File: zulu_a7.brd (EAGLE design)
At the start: 61 x 25.4 mm, 183 parts, among them J1 Pmod 2x6, Q1 12MHz 25ppm (FPGA + FT2232HQ), Q2 2N7002, Q3 MBT3904DW1T1, U1 XC7A35T-1CPG236C, U10 93LC46BT-I/SN, U2 FT2232HQ USB-UART/JTAG Bridge, U3 AS4C32M16SB-6TIN, U4 W25Q128JVSIQ, U8 LTC3569EUDC#TRPBF, X1 Molex 105017-0001 Micro-USB-B

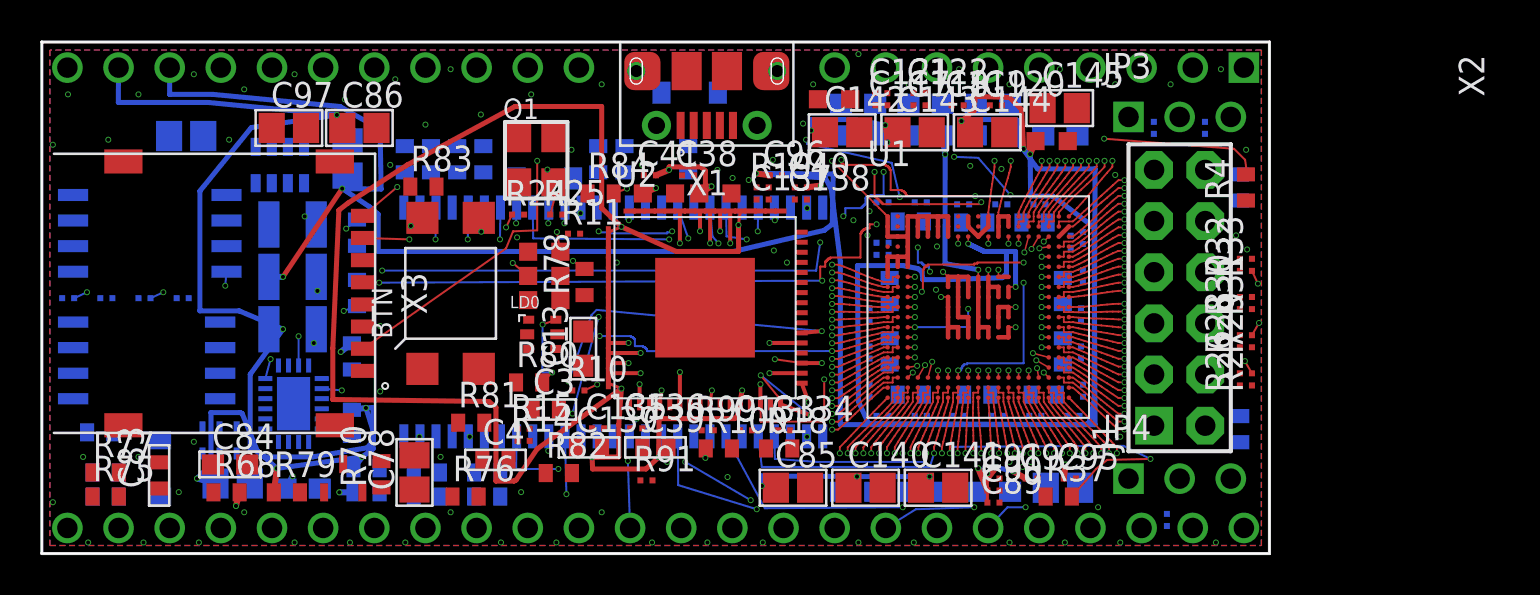
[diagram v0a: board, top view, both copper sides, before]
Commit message: The USB differential pair routes: five faults, each hidden by the one before it
USB_D_P/USB_D_N goes down on L16 at 21.6/21.6 mm, skew 0.921 against a
1.27 mm budget, coupled at exactly 0.2750 mm centre to centre for its whole
length, 0.15 mm conductors, L1 fan-in / L16 coupled / L3 for the side swap.
AIN15 and AIN16 come with it as ordinary single-ended nets, which is right
for XADC inputs at 1 MSPS. 20 of 175 signals bare, against 24; 2620 wires,
408 vias, 0 findings.

Nothing here was congestion. Every one of these was found only after the
previous one stopped masking it.

1. THE FAN-OUT WAS NEVER WIDENED. The two vias at an end sit where their
conductors end, PAIR_W + PAIR_GAP = 0.275 mm apart, and two 0.30 mm vias at
0.09 need 0.390. route_pair's docstring has promised since it was written
that "the fan-out is widened if it does not hold" -- it measured the gap,
reported it and gave up, and the worked example it quoted assumed the older
0.20/0.20 = 0.400 from before PAIR_W and PAIR_GAP were set for 90 ohm.
Every pair on the board died here. The ends are splayed to 0.390 now,
0.0575 mm per conductor, tapering back over the first segment; the coupled
section keeps its gap and its impedance, and an end is coupled to nothing
because it is about to become a via.

2. THE SIDE SWAP WAS COMPUTED AND DISCARDED. crossover() runs for either
branch -- it is what answers a reversed pad order, and this pair has one:
D- is left of D+ at U2 and right of it at X1 -- but only the padlay == lay
branch used the result. The other branch rebuilt A's segments from the
polyline, keeping the exact segment the layer change exists to replace, and
dropped xvias and xsegs. That branch is this pair's case: pads on L1,
coupled on L3. Symptom was "the two conductors come within 0.0000 mm".

3. VIA OWNERSHIP WAS SPLIT BY POSITION. return {pa: vias[:2], pb: vias[2:]}
is right only while each conductor has exactly two vias in that order.
Adding the crossover's broke it silently: USB_D_N came out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
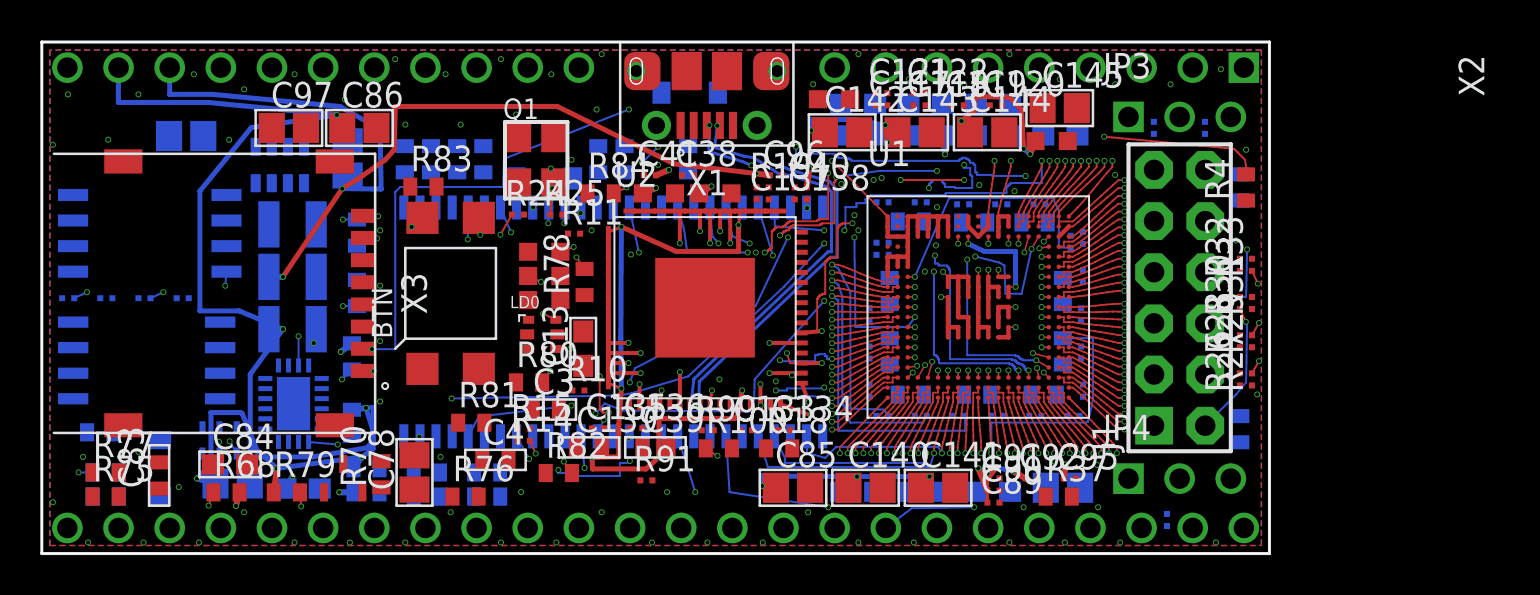
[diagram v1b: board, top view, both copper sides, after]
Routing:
- net VCC1V8: track 221.6 -> 144.0 mm
- net CHAN27: track 67.8 -> 4.05 mm, vias 3 -> 1
- net CHAN19: track 65.9 -> 3.09 mm, vias 5 -> 1
- net CHAN20: track 61.3 -> 3.91 mm, vias 5 -> 1
- net CHAN22: track 2.96 -> 57.8 mm, vias 1 -> 4
- net CHAN11: track 51.7 -> 0.35 mm, vias 4 -> 1
- net JA7: track 0.71 -> 46.1 mm, vias 1 -> 5
- net SD-CLK: track 45.2 -> 0.35 mm, vias 5 -> 1
- net FT-VCORE: track 77.7 -> 35.6 mm
- net CHAN21: track 0.35 -> 39.0 mm, vias 1 -> 4
- net SW2_NET: track 37.3 -> 0.00 mm, vias 2 -> 0
- net ANALOG-IO1: track 0.00 -> 34.9 mm, vias 0 -> 1
- net SD-DAT2: track 0.35 -> 34.6 mm, vias 1 -> 4
- net CHAN6: track 0.35 -> 33.9 mm, vias 1 -> 4
- net FB2_NODE: track 0.00 -> 31.5 mm, vias 0 -> 4
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
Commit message: VU, VEXT and USB5V0 route: eight rails close, and the obstacle models agree
All eight rails now go down -- VCC1V0, VCC1V8, FT-VCORE, FT-VPHY, FT-VPLL,
VU (166.7 mm), VEXT (42.5) and USB5V0 (44.8), 0 edges failed on any of them.
16 of 175 signals bare, against 20; 3031 wires, 423 vias, 0 findings.

Almost none of this was congestion. Seven of the eight faults were a router
carrying its own private model of the board with a category missing from it,
and check_board -- which builds its model from the finished article -- caught
every one.

U8 GETS A FAN-OUT. VU arrives on six pins of a QFN-20 at 0.5 mm pitch and
there is room beside it for two vias, so four were stranded every run.
escape_qfn's POWERNET skip is right for a rail that ends on a pour and wrong
for one power.py must reach with a discrete via and cannot; QFN_POWER names
the exceptions. Daisy-chaining is not a substitute -- a stub from one VIN pin
to the next runs straight through the pins of other nets in between, so the
bus has to leave the pad ring first, which is what this file is for. Fanning
U8 out also escapes its signal pins, which the rest group had been failing on.

THE DAISY CHAIN WALKS. It looked once at each stranded pad, only ever at this
net's VIAS, and stopped at 2.00 mm -- which cannot express the case it is
most needed for. U8's stranded pins are a chain of 2.25, 1.50 and 2.33 mm
hops ending on a pin that has a via. Every link short; only the walk missing.
A pad it has just chained is an anchor for the next, because the stub put it
on the net.

A PAD ALREADY WIRED TO THE NET NEEDS NOTHING. The test was "is one of this
net's vias AT this pad", which predates anything fanning out a package.
escape_qfn leaves a pad wired by a stub to a via 1.00 or 1.60 mm off, and
power.py went on demanding a via of its own beside it, reporting five of U8's
six VU pins unreachable while looking straight at the copper that reached them.

L4 IS IN PWR_PREF. It stopped being a ground plane on 2026-08-27 and nothin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
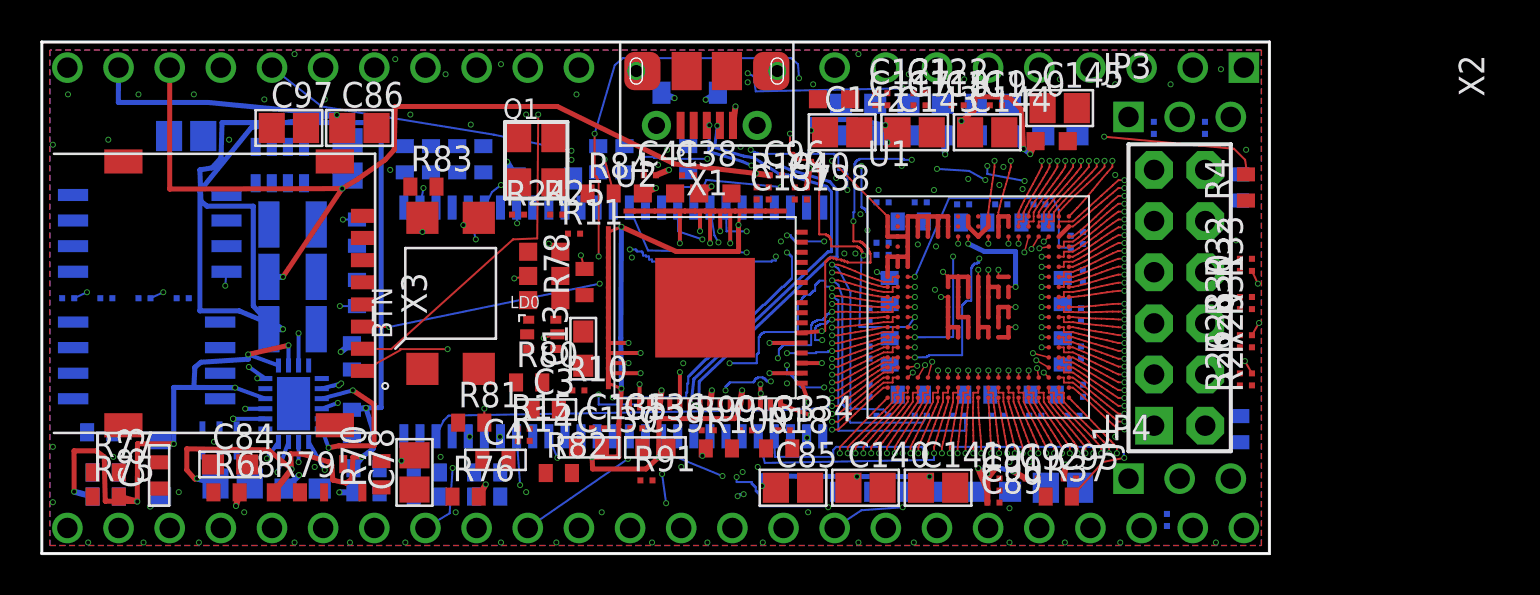
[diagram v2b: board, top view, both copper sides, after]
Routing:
- net VU: track 0.00 -> 166.7 mm, vias 0 -> 12
- net D7: track 59.5 -> 0.71 mm, vias 4 -> 1
- net CHAN18: track 4.07 -> 53.9 mm, vias 1 -> 8
- net SD-CMD: track 0.35 -> 47.9 mm, vias 1 -> 6
- net CHAN11: track 0.35 -> 46.2 mm, vias 1 -> 6
- net JA7: track 46.1 -> 0.71 mm, vias 5 -> 1
- net A4: track 0.35 -> 45.2 mm, vias 1 -> 5
- net USB5V0: track 0.00 -> 44.8 mm, vias 0 -> 2
- net VEXT: track 0.00 -> 42.5 mm, vias 0 -> 2
- net CLK-12M-SHARED: track 41.0 -> 0.00 mm, vias 3 -> 0
- net SD-DAT1: track 42.8 -> 4.00 mm, vias 6 -> 1
- net CHAN21: track 39.0 -> 0.35 mm, vias 4 -> 1
- net SD-DAT0: track 37.9 -> 0.81 mm, vias 5 -> 1
- net A8: track 0.35 -> 36.2 mm, vias 1 -> 6
- net ANALOG-IO1: track 34.9 -> 0.00 mm, vias 1 -> 0
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
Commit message: U2's footprint shorted 30 pin pairs, and the drill rule was missing everywhere
Fusion's DRC reported 727 errors on a board check_board.py called clean. It
was right and this toolchain was wrong in three separate ways.

U2'S QFN-64 FOOTPRINT SHORTS ADJACENT PINS. FT2232HQ-QFN64 has dx and dy
swapped on two of its four edges: the north pads sit at 0.5 mm pitch along x
and were 0.6 mm wide, overlapping BOTH neighbours by 0.1 mm, and the west
pads do the same along y. 16 + 16 pads, 30 shorted pairs, in copper, in the
library. South and east are correct, which is why it survived -- three edges
of four look right and the two wrong ones are wrong in opposite directions,
so nothing about the outline or the pin count looks off. Fixed in the
schematic; all four edges now agree. Every other package was audited and
none has same-layer overlapping pads. MINI_MELF-0102AX looked like a second
case and is not: its two pads are at one point on layers 1 and 16, and no
part is fitted with it.

THE DRILL RULE APPLIED TO NOTHING. VIA_PITCH was 0.39 = VIA_L + clr, two
0.30 lands at 0.09 -- the COPPER rule, and the only rule any of these tools
knew. mdDrill wants 0.20 mm between HOLE EDGES, which on 0.2 mm drills is
0.40 mm centre to centre, so the fan-out ring sat 0.010 mm inside it on all
93 of its adjacent pairs. escape.via_sep(clr) is max of the two now and the
moat, the ring, power.py and signals.py all use it; the escape still closes,
103 vias needing 41.2 mm of a 58.08 mm perimeter.

The distinction matters beyond that number. EVERY clearance test here skips
same-net pairs, correctly -- two traces of one signal may touch. A drill is
not copper. It is a mechanical operation and the rule holds whoever owns the
hole, which is exactly how EN_BIAS ended up with two vias 0.010 mm apart and
SW2_NET with two overlapping by 0.048: a signals.py via landing on top of an
escape_qfn one, same net, so nothing looked. Those now SNAP -- the duplicate
is dropped and the route moved onto the via tha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
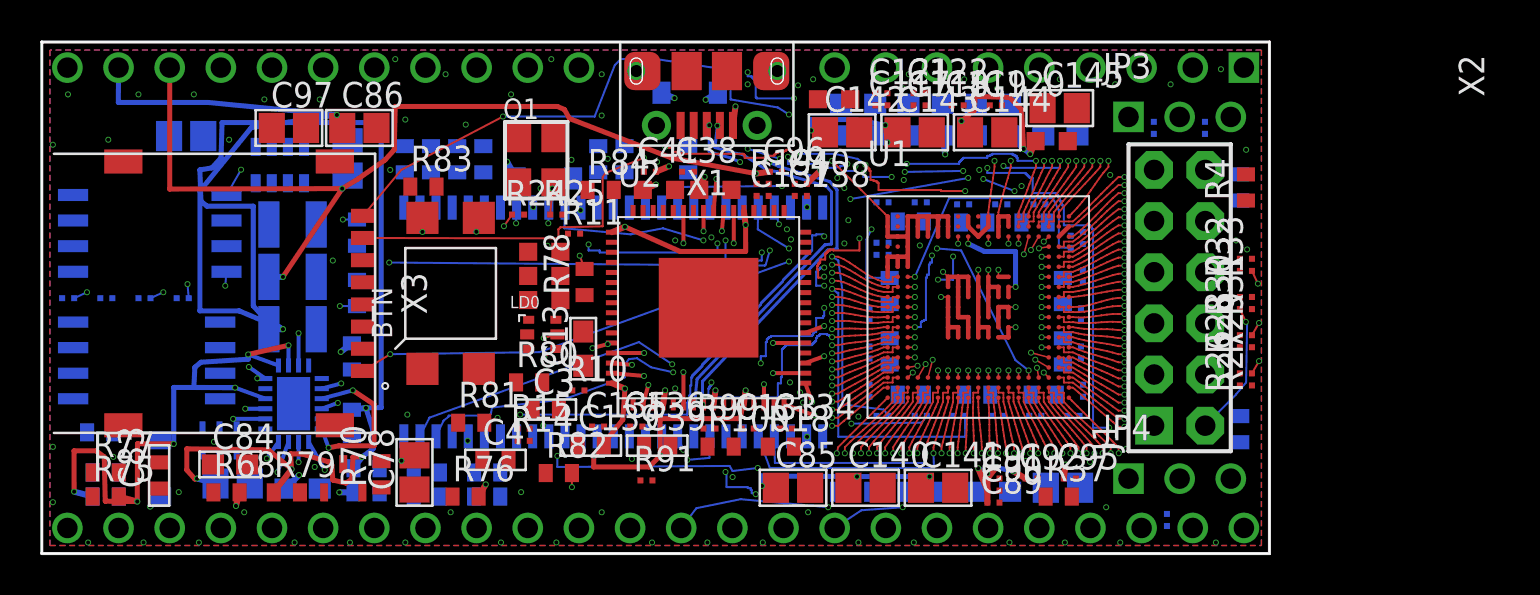
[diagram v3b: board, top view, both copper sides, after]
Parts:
- moved C137 0.18 mm to (35.8, 17.8)
- moved C138 0.18 mm to (37.7, 17.8)
- moved C40 0.18 mm to (37.7, 18.4)
- moved L4 0.18 mm to (30.6, 18.1)
- moved L5 0.18 mm to (33.4, 18.1)
- moved R19 0.18 mm to (35.8, 18.4)
- moved R84 0.18 mm to (27.7, 18.1)
- moved C38 0.17 mm to (32.1, 19.0)
- moved C41 0.17 mm to (30.2, 19.0)
- moved C96 0.17 mm to (36.4, 19.0)
- moved U2 0.17 mm to (33.1, 12.2)
- moved R100 0.12 mm to (33.7, 5.31)
- moved C133 0.12 mm to (35.1, 6.21)
- moved C134 0.12 mm to (36.9, 6.21)
- moved R99 0.12 mm to (33.2, 6.21)
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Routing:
- net D4: track 0.81 -> 98.6 mm, vias 1 -> 6
- net CHAN24: track 60.4 -> 0.35 mm, vias 4 -> 1
- net DONE: track 58.1 -> 1.00 mm, vias 7 -> 1
- net CHAN15: track 15.9 -> 71.3 mm, vias 2 -> 5
- net EE-CS: track 1.60 -> 52.3 mm, vias 1 -> 3
- net CHAN18: track 53.9 -> 4.09 mm, vias 8 -> 1
- net SD-DAT3: track 52.0 -> 3.19 mm, vias 4 -> 1
- net SD-CMD: track 47.9 -> 0.35 mm, vias 6 -> 1
- net CHAN22: track 49.0 -> 2.96 mm, vias 2 -> 1
- net A4: track 45.2 -> 0.35 mm, vias 5 -> 1
- net SD-DAT1: track 4.00 -> 48.1 mm, vias 1 -> 4
- net RAS#: track 22.5 -> 65.6 mm, vias 2 -> 7
- net SD-DAT0: track 0.81 -> 43.9 mm, vias 1 -> 7
- net A12: track 0.35 -> 40.6 mm, vias 1 -> 10
- net JA7: track 0.71 -> 40.8 mm, vias 1 -> 5
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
